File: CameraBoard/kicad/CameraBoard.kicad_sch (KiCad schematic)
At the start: 56 parts, among them Q1 SUD08P06-155L, Q2 SUD08P06-155L, Q3 SUD08P06-155L, U1 LM2678SD-12/NOPB, U2 MP2659GQ-0000-Z

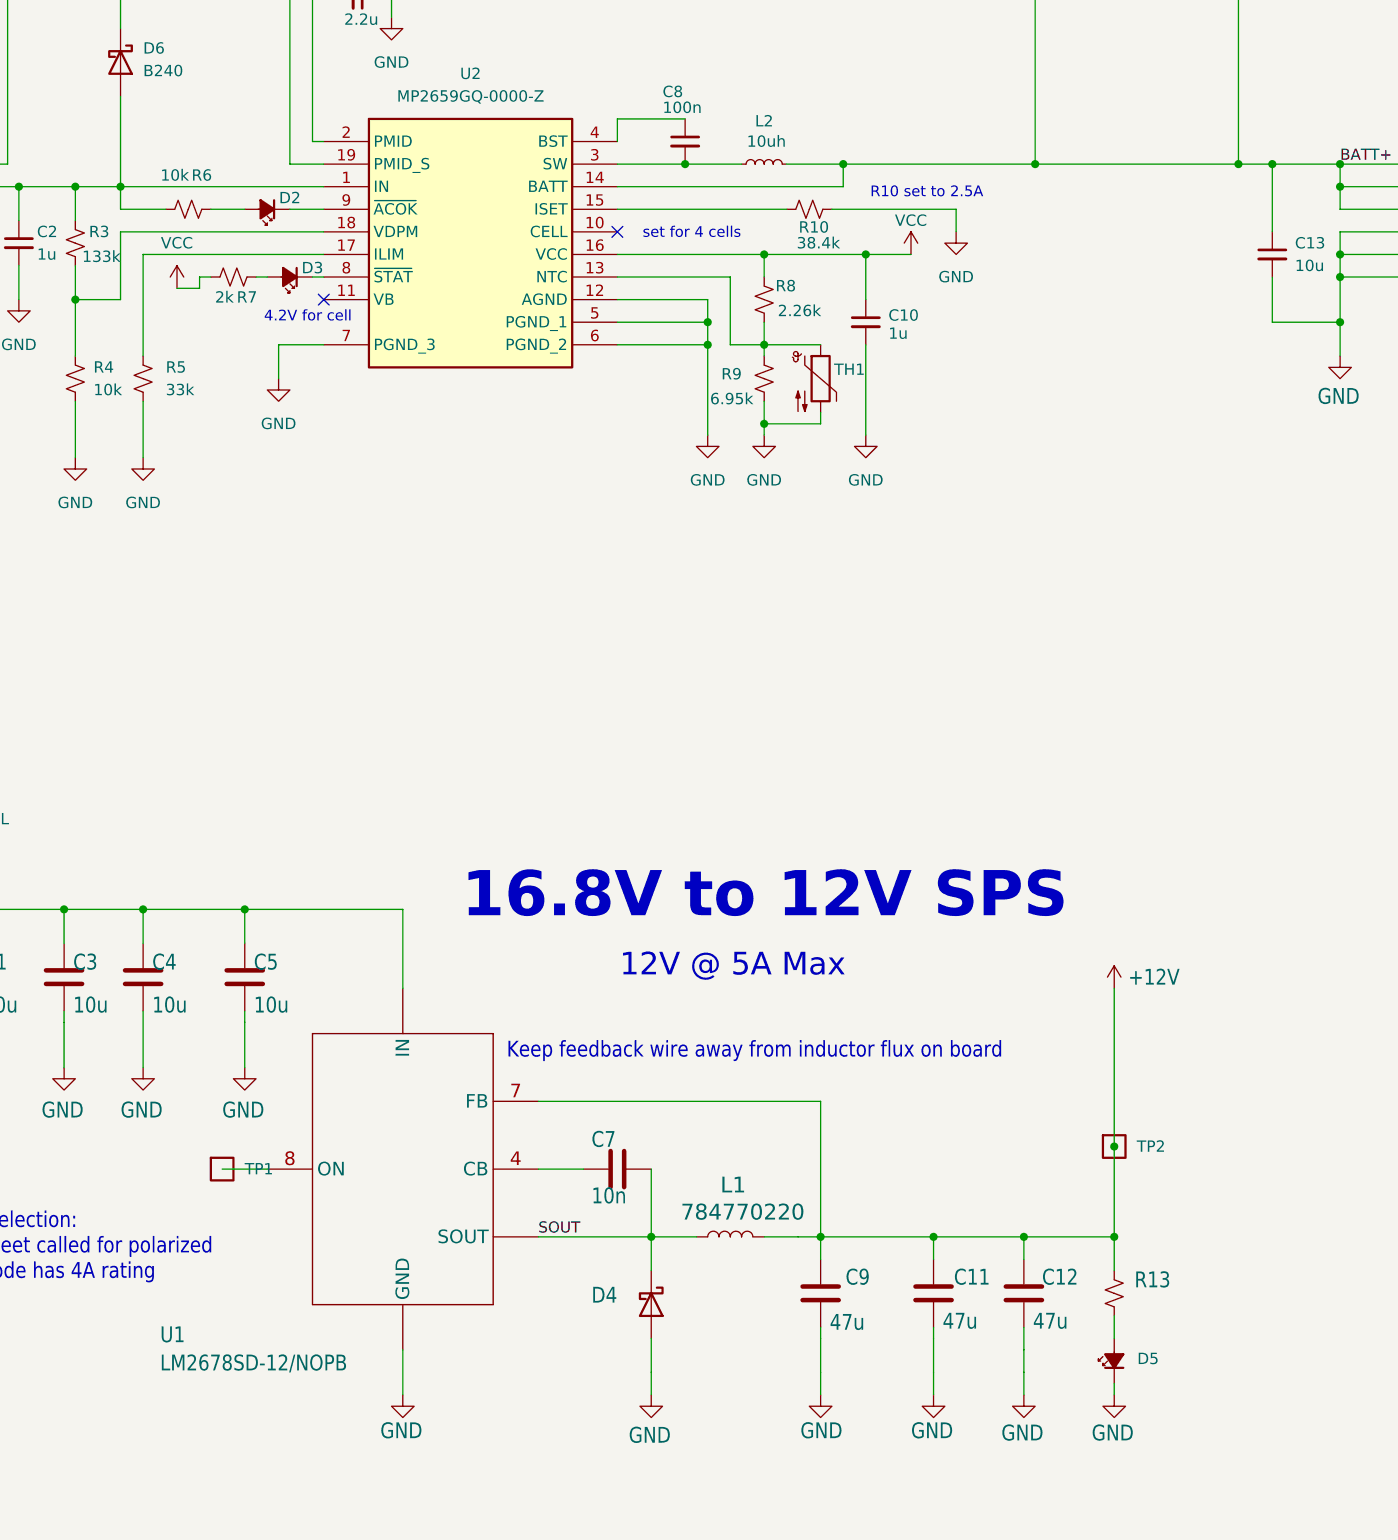
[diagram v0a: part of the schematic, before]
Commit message: Small Updates to PCB
-Fixed zone issue
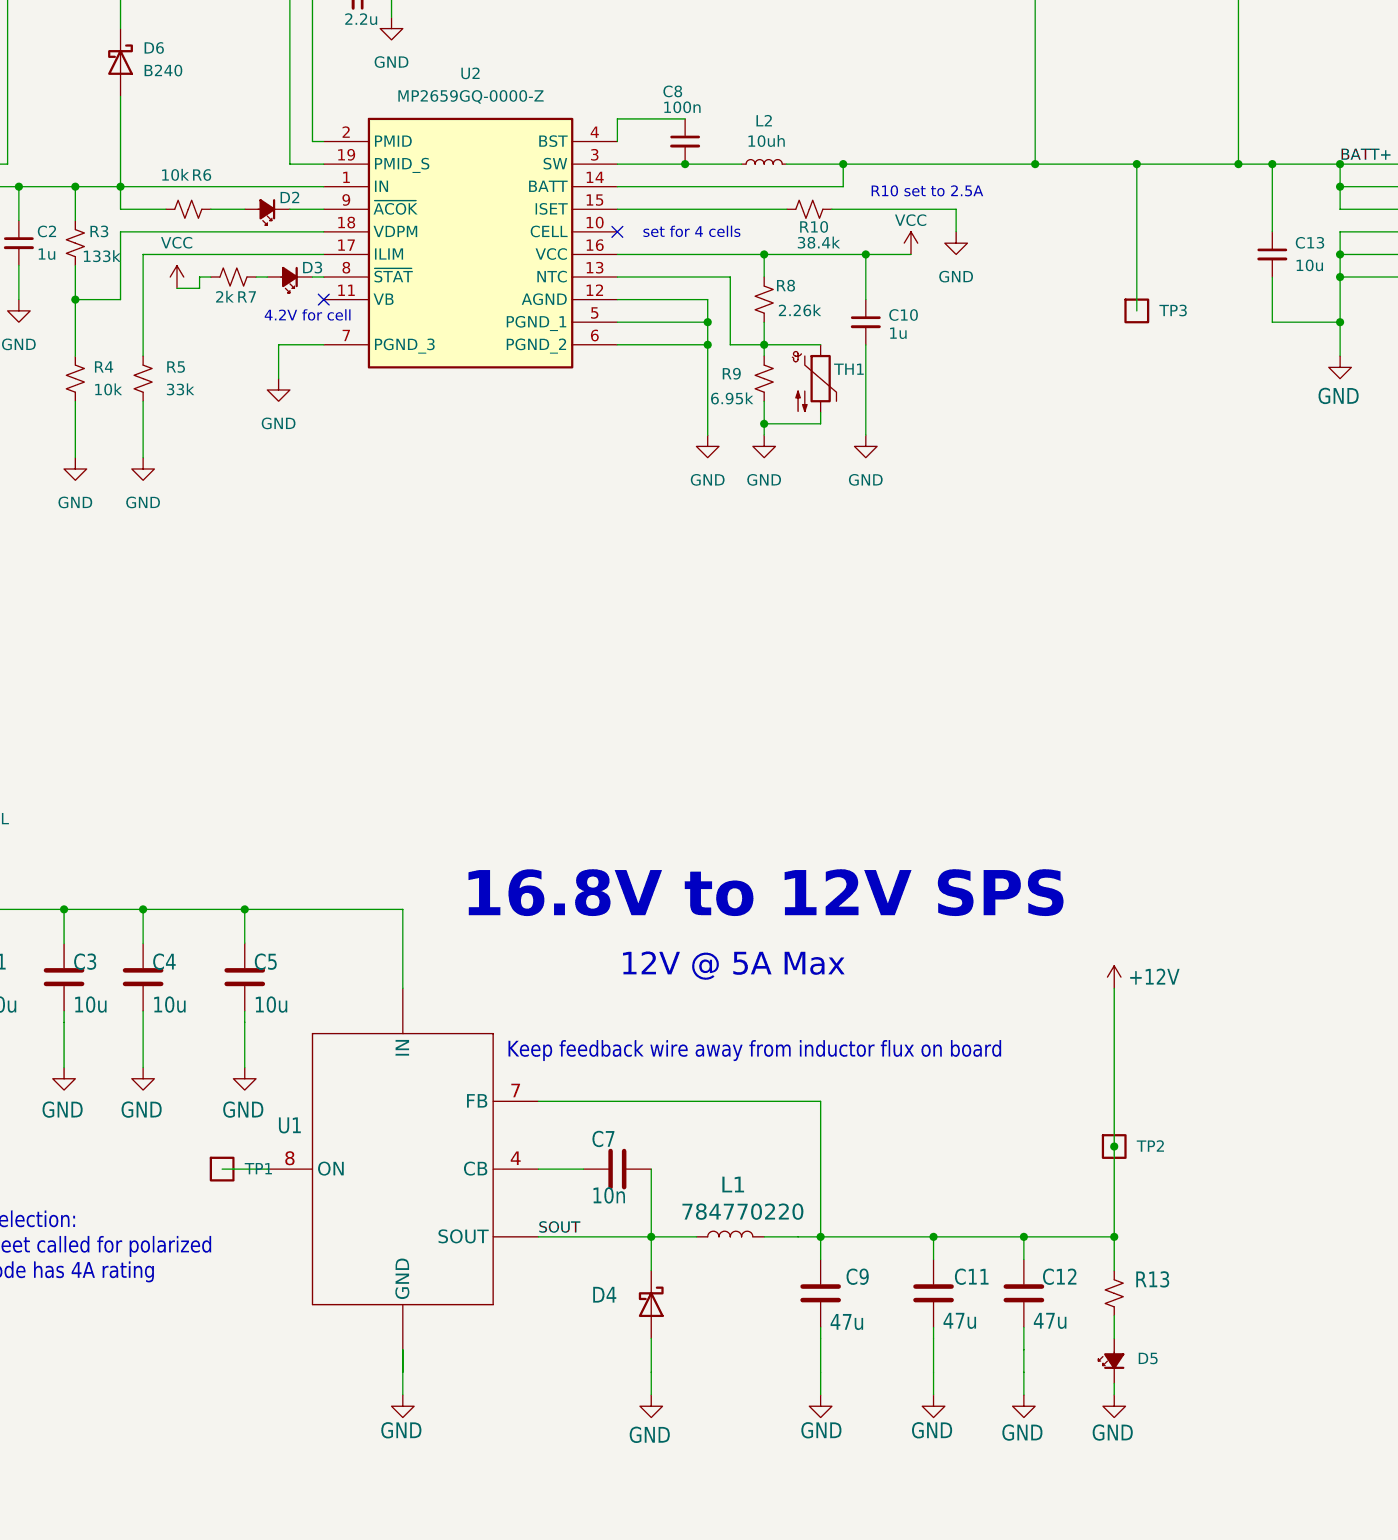
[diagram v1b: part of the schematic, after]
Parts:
- added TP3: Test-Point, CameraBoard:2MM-TEST-POINT, symbol psas-testpoint:Test-Point
- U1: value LM2678SD-12/NOPB -> (none)
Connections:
- net BATT+: now also TP3.1
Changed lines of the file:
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@@
 	)
 	(junction
+		(at 208.28 101.6)
+		(diameter 0)
+		(color 0 0 0 0)
+	)
+	(junction
 		(at 87.63 185.42)
 		(diameter 0)
@@
 	(wire
 		(pts
+			(xy 208.28 118.11) (xy 208.28 101.6)
+		)
+		(stroke
+			(width 0)
+			(type default)
+		)
+	)
+	(wire
+		(pts
 			(xy 77.47 198.12) (xy 77.47 203.2)
 		)
@@
 	(wire
 		(pts
+			(xy 208.28 101.6) (xy 219.71 101.6)
+		)
+		(stroke
+			(width 0)
+			(type default)
+		)
+	)
+	(wire
+		(pts
 			(xy 346.71 160.02) (xy 341.63 160.02)
 		)
@@
 	(wire
 		(pts
-			(xy 196.85 101.6) (xy 219.71 101.6)
+			(xy 196.85 101.6) (xy 208.28 101.6)
 		)
 		(stroke
@@
 	(wire
 		(pts
+			(xy 125.73 234.95) (xy 125.73 237.49)
+		)
+		(stroke
+			(width 0)
+			(type default)
+		)
+	)
+	(wire
+		(pts
 			(xy 162.56 121.92) (xy 166.37 121.92)
 		)
@@
 	)
 	(symbol
+		(lib_name "LM2678SD-12/NOPB_1")
+		(lib_id "CameraBoard-eagle-import:LM2678SD-12/NOPB")
+		(at 125.73 214.63 0)
+		(unit 1)
+		(body_style 1)
+		(exclude_from_sim no)
+		(in_bom yes)
+		(on_board yes)
+		(in_pos_files yes)
+		(dnp no)
+		(fields_autoplaced yes)
+		(property "Reference" "U1"
+			(at 113.03 209.7657 0)
+			(show_name no)
+			(do_not_autoplace no)
+			(effects
+				(font
+					(size 1.778 1.5113)
+				)
+			)
+		)
+		(property "Value" ""
+			(at 118.11 209.55 0)
+			(show_name no)
+			(do_not_autoplace no)
+			(effects
+				(font
+					(size 1.778 1.5113)
+				)
+				(justify left bottom)
+			)
+		)
+		(property "Footprint" "CameraBoard:LM2678SD-12_NOPB"
+			(at 125.73 214.63 0)
+			(hide yes)
+			(show_name no)
+			(do_not_autoplace no)
+			(effects
+				(font
+					(size 1.27 1.27)
+				)
+			)
+		)
+		(property "Datasheet" ""
+			(at 125.73 214.63 0)
+			(hide yes)
+			(show_name no)
+			(do_not_autoplace no)
+			(effects
+				(font
+					(size 1.27 1.27)
+				)
+			)
+		)
+		(property "Description" ""
+			(at 125.73 214.63 0)
+			(hide yes)
+			(show_name no)
+			(do_not_autoplace no)
+			(effects
+				(font
+					(size 1.27 1.27)
+				)
+			)
+		)
+		(pin "3"
+		)
+		(pin "12"
+		)
+		(pin "7"
+		)
+		(pin "DAP"
+		)
+		(pin "1"
+		)
+		(pin "5"
+		)
+		(pin "6"
+		)
+		(pin "10"
+		)
+		(pin "8"
+		)
+		(pin "11"
+		)
+		(pin "9"
+		)
+		(pin "2"
+		)
+		(pin "13"
+		)
+		(pin "4"
+		)
+		(pin "14"
+		)
+		(instances
+			(project "CameraBoard"
+				(path "/876601fa-fbd1-4e2d-9c28-84441865735b"
+					(reference "U1")
+					(unit 1)
+				)
+			)
+		)
+	)
+	(symbol
 		(lib_id "Device:C_Small")
 		(at 120.65 82.55 270)
@@
 	)
 	(symbol
-		(lib_id "CameraBoard-eagle-import:LM2678SD-12/NOPB")
-		(at 125.73 214.63 0)
-		(unit 1)
-		(body_style 1)
-		(exclude_from_sim no)
-		(in_bom yes)
-		(on_board yes)
-		(in_pos_files yes)
-		(dnp no)
-		(property "Reference" "U1"
-			(at 98.425 234.315 0)
-			(show_name no)
-			(do_not_autoplace no)
-			(effects
-				(font
-					(size 1.778 1.5113)
-				)
-				(justify left bottom)
-			)
-		)
-		(property "Value" "LM2678SD-12/NOPB"
-			(at 98.425 237.49 0)
-			(show_name no)
-			(do_not_autoplace no)
-			(effects
-				(font
-					(size 1.778 1.5113)
-				)
-				(justify left bottom)
-			)
-		)
-		(property "Footprint" "CameraBoard:LM2678SD-12_NOPB"
-			(at 125.73 214.63 0)
-			(hide yes)
-			(show_name no)
-			(do_not_autoplace no)
-			(effects
-				(font
-					(size 1.27 1.27)
-				)
-			)
-		)
-		(property "Datasheet" ""
-			(at 125.73 214.63 0)
-			(hide yes)
-			(show_name no)
-			(do_not_autoplace no)
-			(effects
-				(font
-					(size 1.27 1.27)
-				)
-			)
-		)
-		(property "Description" ""
-			(at 125.73 214.63 0)
-			(hide yes)
-			(show_name no)
-			(do_not_autoplace no)
-			(effects
-				(font
-					(size 1.27 1.27)
-				)
-			)
-		)
-		(property "DIS" ""
-			(at 125.73 214.63 0)
-			(hide yes)
-			(show_name no)
-			(do_not_autoplace no)
-			(effects
-				(font
-					(size 1.27 1.27)
-				)
-			)
-		)
-		(property "DPN" ""
-			(at 125.73 214.63 0)
-			(hide yes)
-			(show_name no)
-			(do_not_autoplace no)
-			(effects
-				(font
-					(size 1.27 1.27)
-				)
-			)
-		)
-		(property "MAN" ""
-			(at 125.73 214.63 0)
-			(hide yes)
-			(show_name no)
-			(do_not_autoplace no)
-			(effects
-				(font
-					(size 1.27 1.27)
-				)
-			)
-		)
-		(property "MPN" ""
-			(at 125.73 214.63 0)
-			(hide yes)
-			(show_name no)
-			(do_not_autoplace no)
-			(effects
-				(font
-					(size 1.27 1.27)
-				)
-			)
-		)
-		(property "Sim.Device" ""
-			(at 125.73 214.63 0)
-			(hide yes)
-			(show_name no)
-			(do_not_autoplace no)
-			(effects
-				(font
-					(size 1.27 1.27)
-				)
-			)
-		)
-		(pin "8"
-		)
-		(pin "2"
-		)
-		(pin "3"
-		)
-		(pin "9"
-		)
-		(pin "DAP"
-		)
-		(pin "7"
-		)
-		(pin "4"
-		)
-		(pin "12"
-		)
-		(pin "13"
-		)
-		(pin "14"
-		)
-		(instances
-			(project "CameraBoard"
-				(path "/876601fa-fbd1-4e2d-9c28-84441865735b"
-					(reference "U1")
-					(unit 1)
-				)
-			)
-		)
-	)
-	(symbol
 		(lib_id "Device:R_Small_US")
 		(at 196.85 50.8 90)
@@
 					(unit 1)
 				)
+			)
+		)
+	)
+	(symbol
+		(lib_id "psas-testpoint:Test-Point")
+		(at 208.28 118.11 0)
+		(unit 1)
+		(body_style 1)
+		(exclude_from_sim no)
+		(in_bom yes)
+		(on_board yes)
+		(in_pos_files yes)
+		(dnp no)
+		(fields_autoplaced yes)
+		(property "Reference" "TP3"
+			(at 210.82 118.1099 0)
+			(show_name no)
+			(do_not_autoplace no)
+			(effects
+				(font
+					(size 1.27 1.27)
+				)
+				(justify left)
+			)
+		)
+		(property "Value" "Test-Point"
+			(at 208.28 115.57 0)
+			(hide yes)
+			(show_name no)
+			(do_not_autoplace no)
+			(effects
+				(font
+					(size 1.27 1.27)
+				)
+			)
+		)
+		(property "Footprint" "CameraBoard:2MM-TEST-POINT"
+			(at 208.28 115.57 0)
+			(hide yes)
+			(show_name no)
+			(do_not_autoplace no)
+			(effects
+				(font
+					(size 1.27 1.27)
+				)
+			)
+		)
+		(property "Datasheet" ""
+			(at 208.28 115.57 0)
+			(hide yes)
+			(show_name no)
+			(do_not_autoplace no)
+			(effects
+				(font
+					(size 1.27 1.27)
+				)
+			)
+		)
+		(property "Description" ""
+			(at 208.28 118.11 0)
+			(hide yes)
+			(show_name no)
+			(do_not_autoplace no)
+			(effects
+				(font
+					(size 1.27 1.27)
+				)
+			)
+		)
+		(pin "1"
+		)
+		(instances
+			(project "CameraBoard"
+				(path "/876601fa-fbd1-4e2d-9c28-84441865735b"
+					(reference "TP3")
+					(unit 1)
+				)

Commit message: Updates to BOM and Footprints
-Inductor and thermistor had wrong footprints
-Had to change layout and reroute traces for footprints
-Filled out BOM from schematic
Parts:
- C1, C3, C4, C5: footprint CameraBoard:.0805-B-NOSILK -> oresat-passives:0805-C-NOSILK; DIS (none) -> Digikey; DPN (none) -> 490-GRT21BC71E106KE13KCT-ND; MPN (none) -> GRT21BC71E106KE13K; Manufacturer_Name (none) -> Murata Electronics
- C10: footprint Capacitor_SMD:C_0603_1608Metric -> oresat-passives:0603-C-NOSILK; DIS (none) -> Digikey; DPN (none) -> 490-GRT188R71E105KE13DCT-ND; MPN (none) -> GRT188R71E105KE13D; Manufacturer_Name (none) -> Murata Electronics
- C11, C12, C9: footprint CameraBoard:1206-A -> oresat-passives:1206-C; DIS (none) -> Digikey; DPN (none) -> 490-5528-1-ND; MPN (none) -> GRM31CR61A476ME15L; Manufacturer_Name (none) -> Murata Electronics
- C13: footprint Capacitor_SMD:C_1206_3216Metric -> oresat-passives:1206-C; DIS (none) -> Digikey; DPN (none) -> 445-12883-1-ND; MPN (none) -> CGA5L3X5R1H106M160AB; Manufacturer_Name (none) -> TDK
- C2: footprint Capacitor_SMD:C_0805_2012Metric -> oresat-passives:0805-C-NOSILK; DIS (none) -> Digikey; DPN (none) -> 490-10675-2-ND; MPN (none) -> GCM21BR71H105KA03L; Manufacturer_Name (none) -> Murata Electronics
- C6: footprint Capacitor_SMD:C_1206_3216Metric -> oresat-passives:1206-C; DIS (none) -> Digikey; DPN (none) -> 1276-1072-1-ND; MPN (none) -> CL31B225KAHNNNE; Manufacturer_Name (none) -> Samsung Electro-Mechanics
- C7: footprint CameraBoard:.0603-A-NOSILK -> oresat-passives:0603-C-NOSILK; DIS (none) -> Digikey; DPN (none) -> 399-12983-1-ND; MPN (none) -> C0603C103J5RACAUTO; Manufacturer_Name (none) -> KEMET
- C8: footprint Capacitor_SMD:C_0603_1608Metric -> oresat-passives:0603-C-NOSILK; DIS (none) -> Digikey; DPN (none) -> 399-6856-1-ND; MPN (none) -> C0603C104K5RACAUTO; Manufacturer_Name (none) -> KEMET
- D2, D3, D5: footprint LED_SMD:LED_0603_1608Metric -> oresat-diodes:LED_0603_1608Metric; DIS (none) -> Digikey; DPN (none) -> 732-150060AS75000CT-ND; MPN (none) -> 150060AS75000; Manufacturer_Name (none) -> Wurth
- D4: DIS (none) -> Digikey; DPN (none) -> MBRS340T3GOSCT-ND; MPN (none) -> MBRS340T3G; Manufacturer_Name (none) -> onsemi
- D6: DIS (none) -> Digikey; DPN (none) -> B240A-FDICT-ND; MPN (none) -> B240A-13-F; Manufacturer_Name (none) -> Diodes Incorporated
- JP1, JP2, JP3: DIS (none) -> Digikey; DPN (none) -> 732-5315-ND; MPN (none) -> 61300211121; Manufacturer_Name (none) -> Würth Elektronik
- JP10, JP11, JP12, JP13, JP14, JP5, JP6, JP7, JP8, JP9: DIS (none) -> Digikey; DPN (none) -> 732-5316-ND; MPN (none) -> 61300311121; Manufacturer_Name (none) -> Würth Elektronik
- JP4: DIS (none) -> Digikey; DPN (none) -> 732-5319-ND; MPN (none) -> 61300611121; Manufacturer_Name (none) -> Würth Elektronik
- L1: DIS (none) -> Digikey; DPN (none) -> 732-6785-1-ND; MPN (none) -> 74477110; Manufacturer_Name (none) -> Würth Elektronik
- L2: footprint Inductor_SMD:L_0603_1608Metric -> oresat-misc:WE-PD_1260; DIS (none) -> Digikey; DPN (none) -> 732-1208-1-ND; MPN (none) -> 74477110; Manufacturer_Name (none) -> Würth Elektronik
- Q1, Q2, Q3: DIS (none) -> Digikey; DPN (none) -> SUD08P06-155L-GE3CT-ND; MPN (none) -> SUD08P06-155L-GE3; Manufacturer_Name (none) -> Vishay Siliconix
- R1, R2, R4, R6: footprint Resistor_SMD:R_0603_1608Metric -> oresat-passives:0603-C-NOSILK; DIS (none) -> Digikey; DPN (none) -> RMCF0603FT10K0CT-ND; MPN (none) -> RMCF0603FT10K0; Manufacturer_Name (none) -> Stackpole Electronics
- R10: footprint Resistor_SMD:R_0603_1608Metric -> oresat-passives:0603-C-NOSILK; DIS (none) -> Mouser; DPN (none) -> 71-TNPW060338K8BEEA; MPN (none) -> TNPW060338K8BEEA; Manufacturer_Name (none) -> Vishay
- R11, R12: footprint Resistor_SMD:R_0603_1608Metric -> oresat-passives:0603-C-NOSILK; DIS (none) -> Digikey; DPN (none) -> RMCF0603FT2K70CT-ND; MPN (none) -> RMCF0603FT1K00; Manufacturer_Name (none) -> Stackpole Electronics Inc
- R13: footprint Resistor_SMD:R_0603_1608Metric -> oresat-passives:0603-C-NOSILK; DIS (none) -> Digikey; DPN (none) -> 541-3.30KHCT-ND; MPN (none) -> CRCW06033K30FKEA; Manufacturer_Name (none) -> Vishay Dale
- R14: footprint Resistor_SMD:R_0603_1608Metric -> oresat-passives:0603-C-NOSILK; DIS (none) -> Digikey; DPN (none) -> 13-RC0603FR-10150KLCT-ND; MPN (none) -> RC0603FR-10150KL; Manufacturer_Name (none) -> YAEGO
- R3: footprint Resistor_SMD:R_0603_1608Metric -> oresat-passives:0603-C-NOSILK; DIS (none) -> Digikey; DPN (none) -> 541-133KHCT-ND; MPN (none) -> CRCW0603133KFKEA; Manufacturer_Name (none) -> Vishay Dale
- R5: footprint Resistor_SMD:R_0603_1608Metric -> oresat-passives:0603-C-NOSILK; DIS (none) -> Digikey; DPN (none) -> RMCF0603FT33K0CT-ND; MPN (none) -> RMCF0603FT33K0; Manufacturer_Name (none) -> Stackpole Electronics
- R7: footprint Resistor_SMD:R_0603_1608Metric -> oresat-passives:0603-C-NOSILK; DIS (none) -> Digikey; DPN (none) -> P2.00KHCT-ND; MPN (none) -> ERJ-3EKF2001V; Manufacturer_Name (none) -> Panasonic Industry
- R8: footprint Resistor_SMD:R_0603_1608Metric -> oresat-passives:0603-C-NOSILK; DIS (none) -> Digikey; DPN (none) -> RMCF0603FT3K00CT-ND; MPN (none) -> RMCF0603FT3K00; Manufacturer_Name (none) -> Stackpole Electronics Inc
- R9: footprint Resistor_SMD:R_0603_1608Metric -> oresat-passives:0603-C-NOSILK; DIS (none) -> Digikey; DPN (none) -> MCT06030D6501BP100-ND; MPN (none) -> MCT06030D6501BP100; Manufacturer_Name (none) -> Vishay
- TH1: footprint Resistor_SMD:R_0603_1608Metric -> oresat-misc:THRMC1608X95N; DIS (none) -> Digikey; DPN (none) -> 490-16279-1-ND; MPN (none) -> NCU18XH103F60RB; Manufacturer_Name (none) -> Murata Electronics
- TP1, TP2, TP3: DIS (none) -> Digikey; now left out of the parts list
- U1: DIS (none) -> Digikey; DPN (none) -> LM2678S-ADJ/NOPB-ND; MPN (none) -> LM2678S-ADJ/NOPB; Manufacturer_Name (none) -> Texas Instruments
- U2: DIS (none) -> Digikey; DPN (none) -> 1589-MP2659GQ-0000-ZCT-ND; MPN (none) -> MP2659GQ-0000-Z

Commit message: Small Updates to PCB
- Increased battery trace width
- Created zone for 12V supply
- Moved led resistor outside box
- Rearranged mosfets and capacitors to look nicer
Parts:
- D2, D3, D5: footprint oresat-diodes:LED_0603_1608Metric -> LED_SMD:LED_0603_1608Metric
- renumbered D6 to D1, U2 to U1, U1 to U2
